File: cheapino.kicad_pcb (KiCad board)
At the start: 2 copper layers, 132.5 x 95.1 mm, 59 parts, among them K1 SW_Push, K10 SW_Push, K11 SW_Push, K12 SW_Push, K13 SW_Push, K14 SW_Push, K15 SW_Push, K16 SW_Push, K17 SW_Push, K18 SW_Push, K2 SW_Push, K3 SW_Push, K4 SW_Push, K5 SW_Push, K6 SW_Push, K7 SW_Push, K8 SW_Push, K9 SW_Push, U1 RP2040-Zero

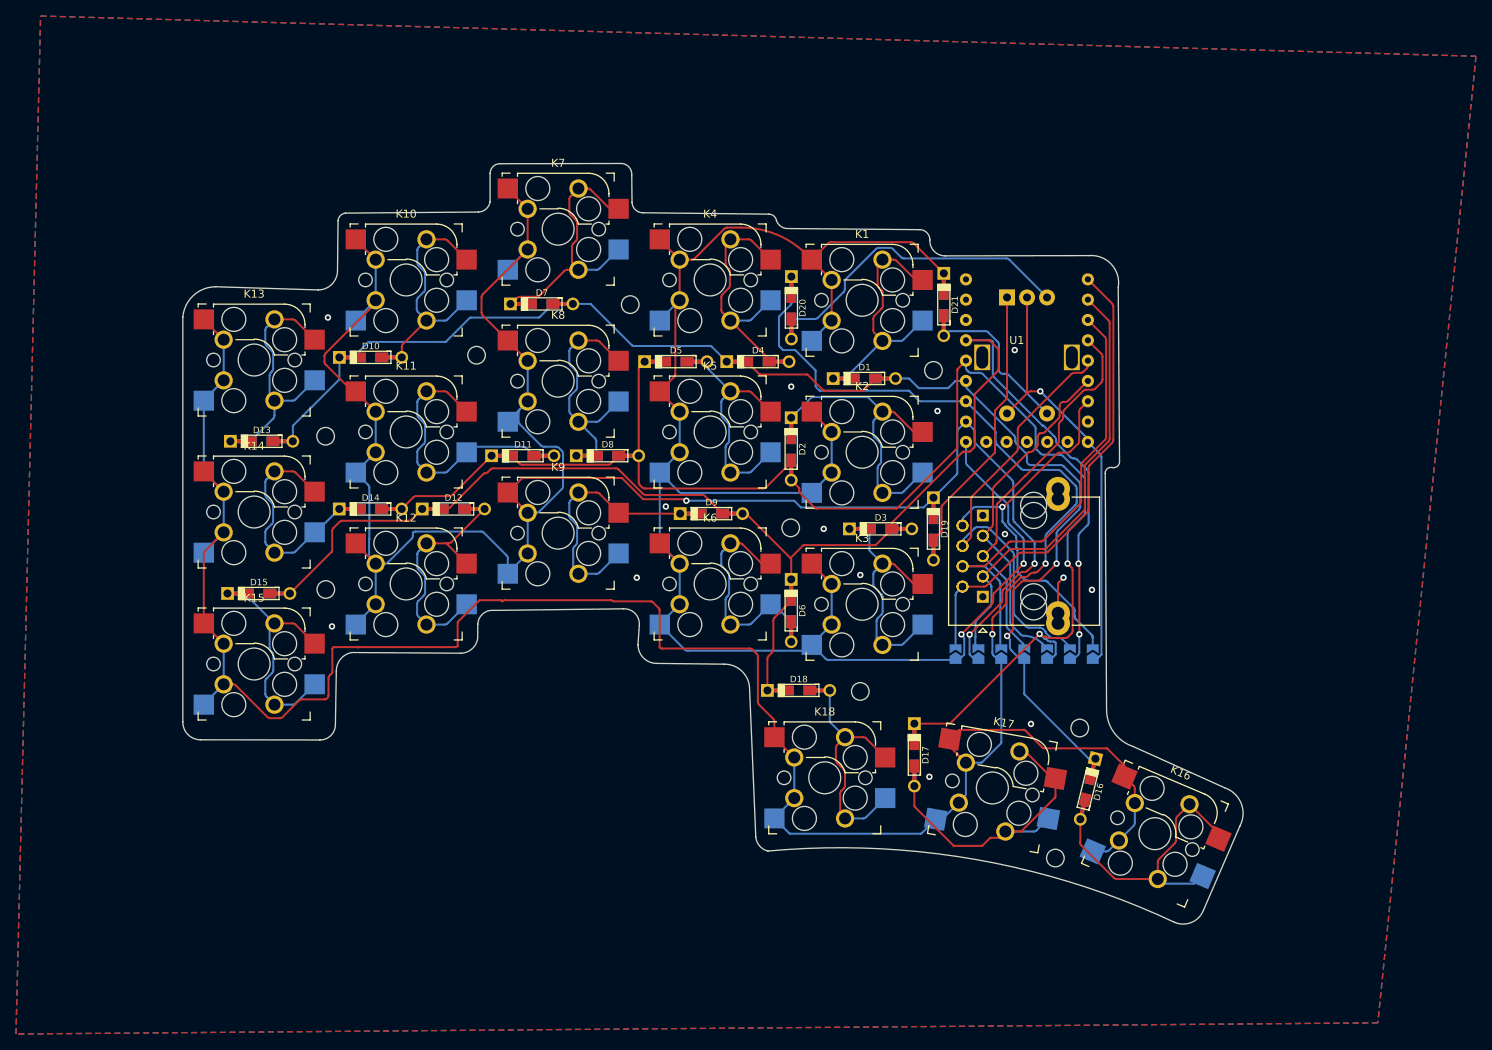
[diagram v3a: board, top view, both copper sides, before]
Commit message: Added logo copper layer, removed some labels
This commit was ordered from jlcpcb
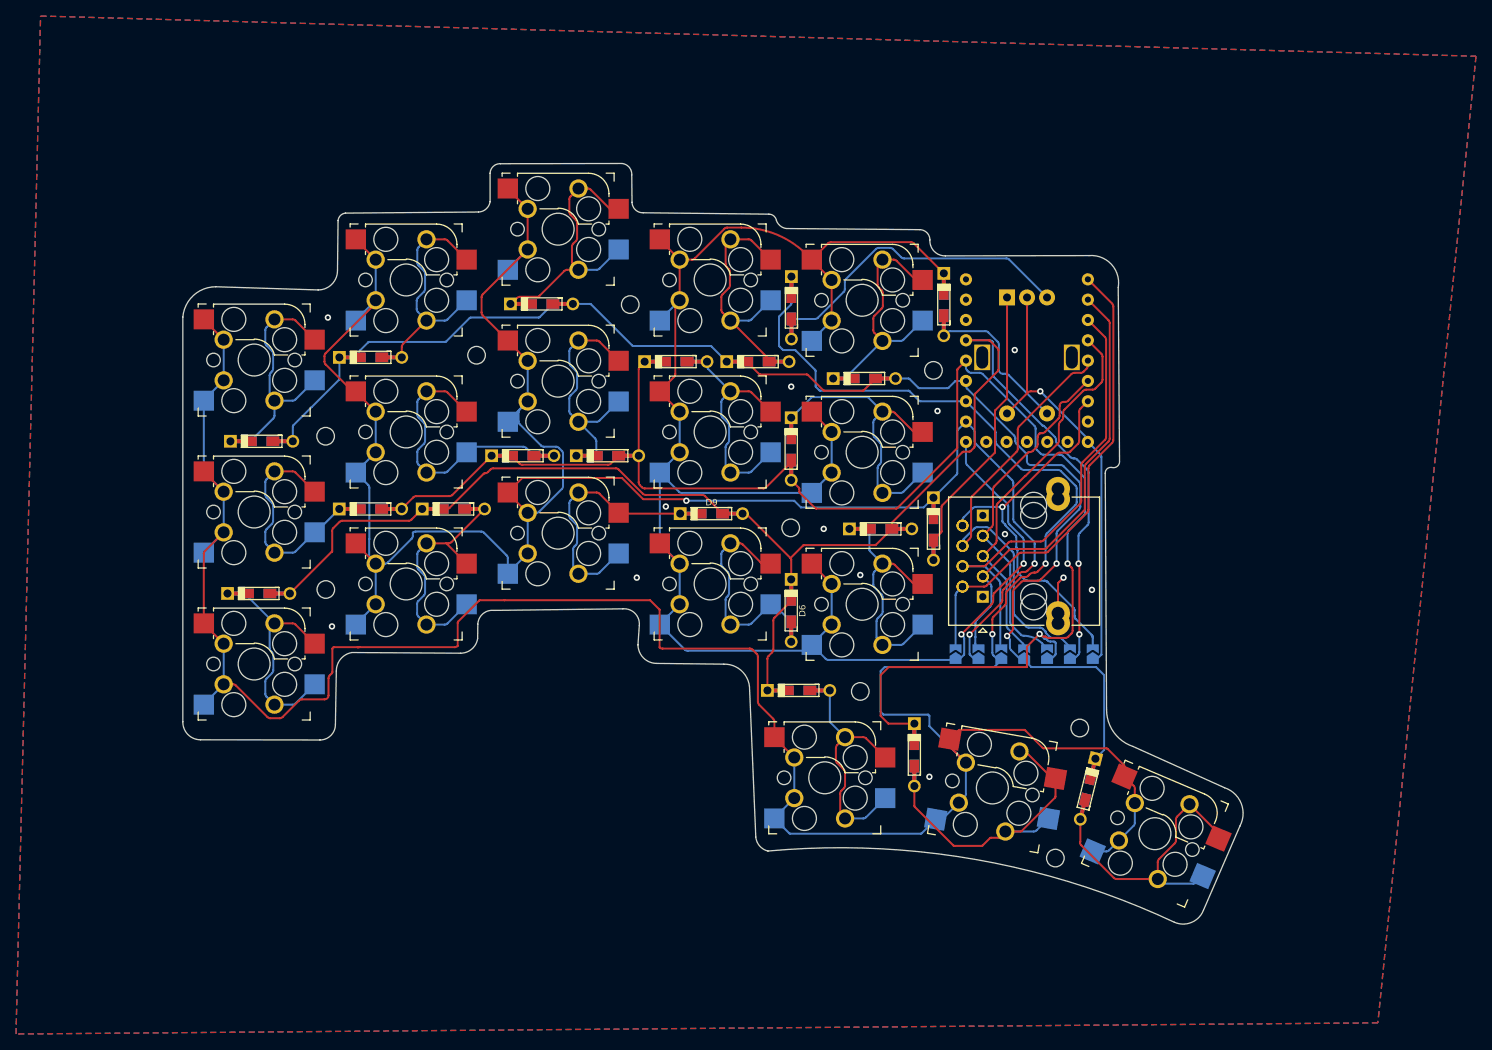
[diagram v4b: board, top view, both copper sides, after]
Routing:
- net COL_3: track 336.5 -> 355.4 mm
- net ROW_2: track 174.8 -> 187.7 mm
- net ROW_1: track 155.4 -> 160.5 mm
- net GND: vias 14 -> 13
